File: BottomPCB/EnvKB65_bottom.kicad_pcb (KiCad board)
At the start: 2 copper layers, 320.8 x 99.3 mm, 7 parts

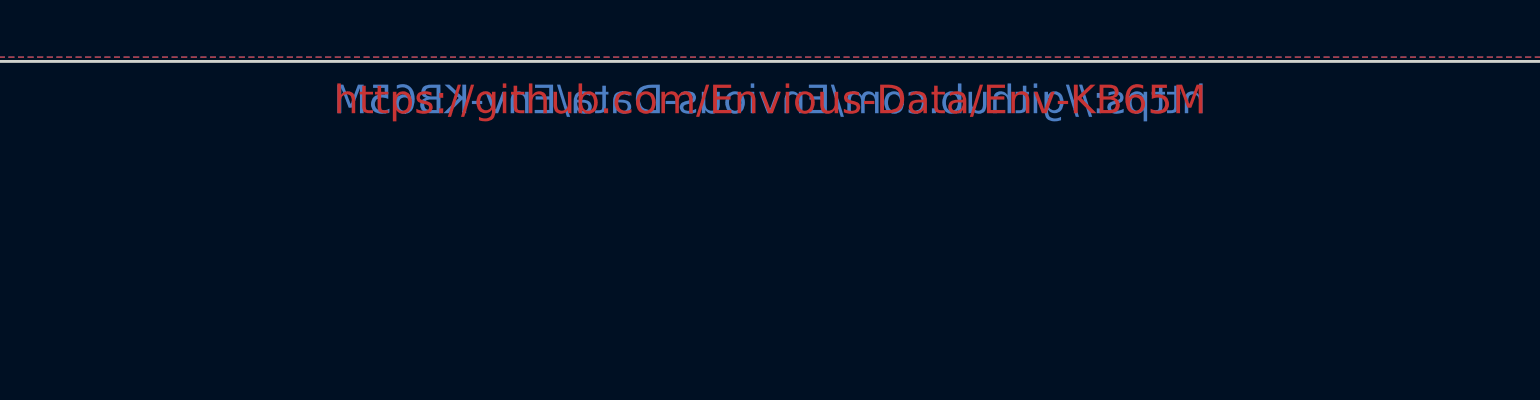
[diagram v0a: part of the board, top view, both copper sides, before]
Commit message: Swapped out mechboads logo for personal order
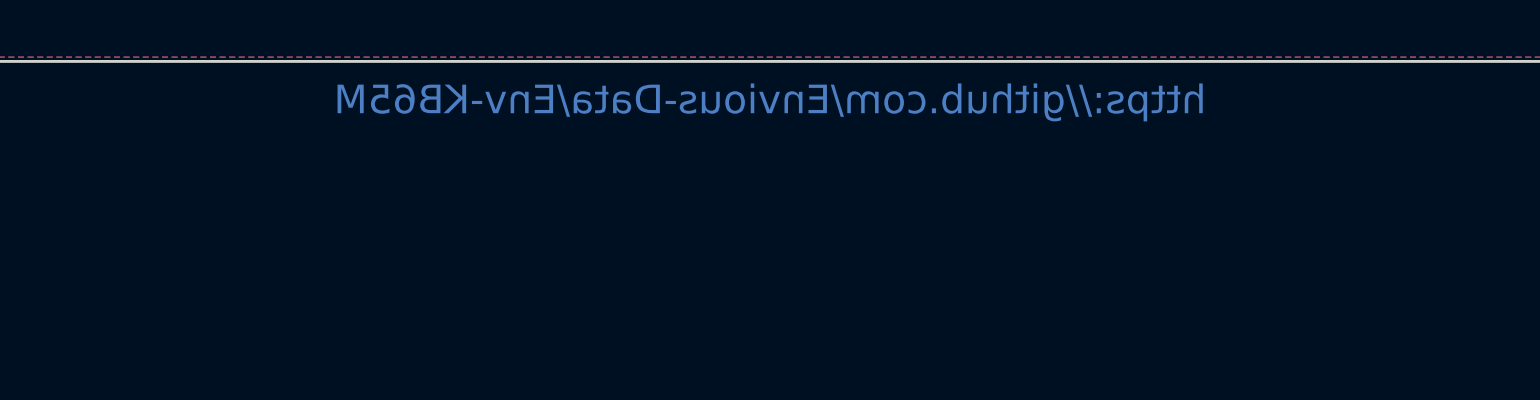
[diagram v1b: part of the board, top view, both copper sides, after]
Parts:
- Ref**: footprint MechboardsLogo:mechboardsLOGO_40mm -> Logo:logo
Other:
- board text added: "http://github.com/Envious-Data/Env-KB65M"
- board text removed: "http://Mechboards.co.uk"

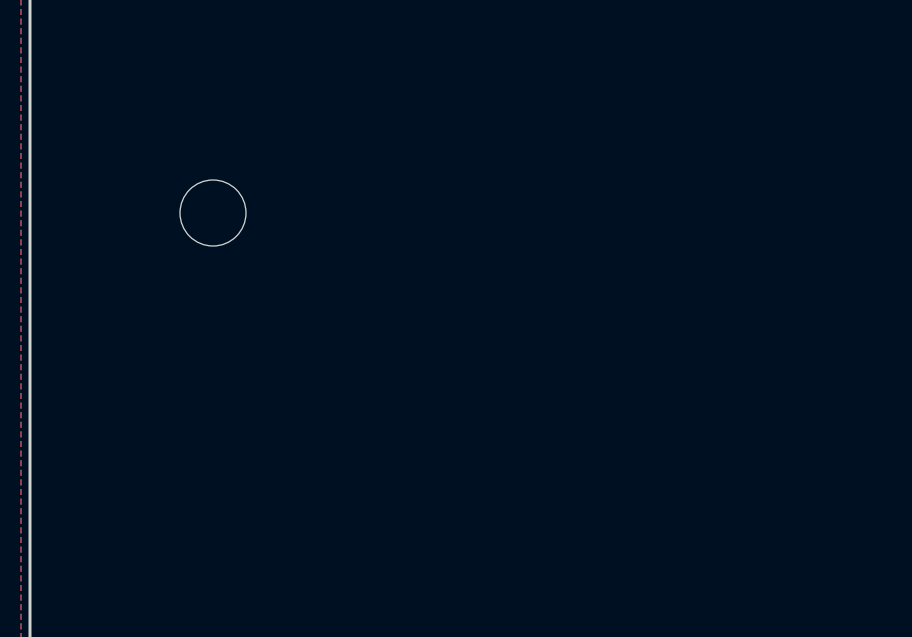
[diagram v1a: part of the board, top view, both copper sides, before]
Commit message: Added ANSI support, generated Gerbers and sent to JLCPCB
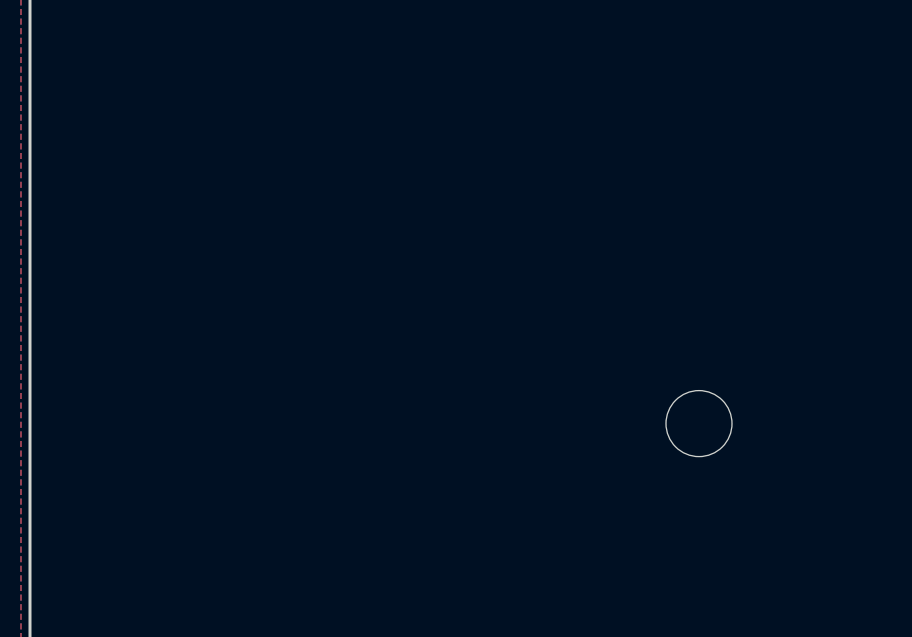
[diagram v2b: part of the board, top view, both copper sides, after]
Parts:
- removed H6: MountingHole, MountingHole:MountingHole_2.2mm_M2
- added H0: MountingHole, MountingHole:MountingHole_2.2mm_M2, F.Cu at (382.2, 101.0)
- moved H1 313.2 mm to (69.0, 101.0)
- moved H3 297.2 mm to (367.8, 180.5)
- moved H4 154.1 mm to (225.0, 122.5)
- moved H2 86.1 mm to (86.8, 185.2)
- moved H5 55.9 mm to (231.2, 178.0)

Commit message: Mount hole tweak to allow for switches to seat properly with a spacer installed
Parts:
- added H1: MountingHole, MountingHole:MountingHole_2.2mm_M2, F.Cu at (382.2, 101.0)
- added H2: MountingHole, MountingHole:MountingHole_2.2mm_M2, F.Cu at (69.0, 101.0)
- added H3: MountingHole, MountingHole:MountingHole_2.2mm_M2, F.Cu at (86.8, 185.2)
- added H6: MountingHole, MountingHole:MountingHole_2.2mm_M2, F.Cu at (210.6, 184.5)
- moved H4 154.1 mm to (367.8, 180.5)
- moved H5 56.5 mm to (224.9, 121.8)
- renumbered H0 to H1, H1 to H2, H2 to H3, H3 to H4
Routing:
- added copper zone on B.Cu, net (none)
- added copper zone on F.Cu, net (none)
- removed copper zone on B.Cu, net GND
- removed copper zone on F.Cu, net GND

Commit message: moved some mount holes a tiny bit and adjusted some traces for wider clearance.
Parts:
- removed the H1 at (382.2, 101.0) (x2)
- removed the H2 at (69.0, 101.0) (x2)
- removed the H3 at (86.8, 185.2) (x2)
- removed the H4 at (367.8, 180.5) (x2)
- removed the H5 at (224.9, 121.8)
- removed the H6 at (210.6, 184.5)
- added H1 (x3): MountingHole, MountingHole:MountingHole_2.2mm_M2, F.Cu at (382.2, 101.0)
- added H2 (x3): MountingHole, MountingHole:MountingHole_2.2mm_M2, F.Cu at (69.0, 101.0)
- added H3 (x3): MountingHole, MountingHole:MountingHole_2.2mm_M2, F.Cu at (86.8, 185.2)
- added H4 (x3): MountingHole, MountingHole:MountingHole_2.2mm_M2, F.Cu at (367.8, 178.2)
- added H5 (x2): MountingHole, MountingHole:MountingHole_2.2mm_M2, F.Cu at (224.9, 121.6)
- added H6 (x2): MountingHole, MountingHole:MountingHole_2.2mm_M2, F.Cu at (210.6, 184.5)
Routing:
- added copper zone on B.Cu, net gnd
- added copper zone on F.Cu, net gnd

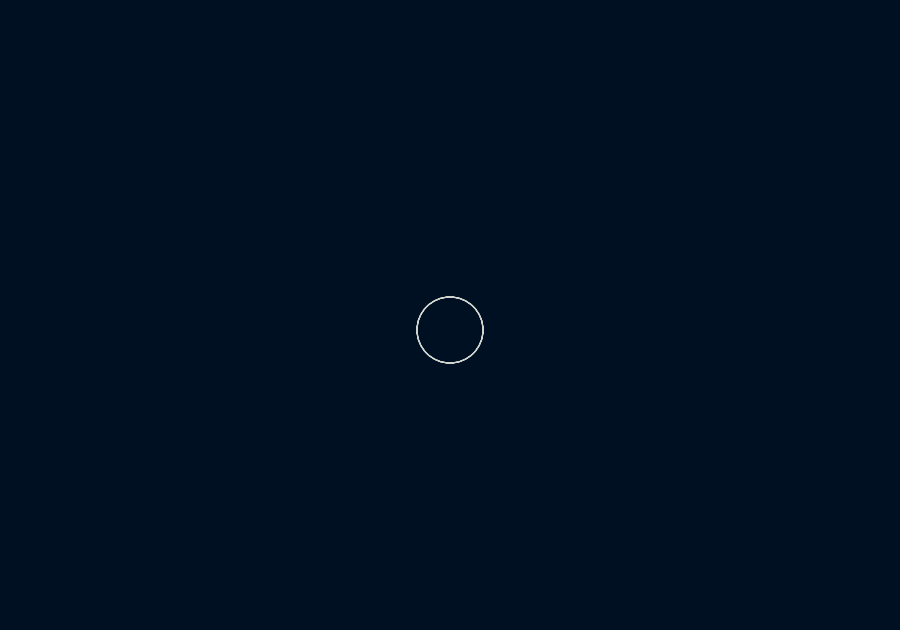
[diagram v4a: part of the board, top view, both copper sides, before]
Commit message: moved mount hole#6 up by 1mm and changed stabilizer cut out.
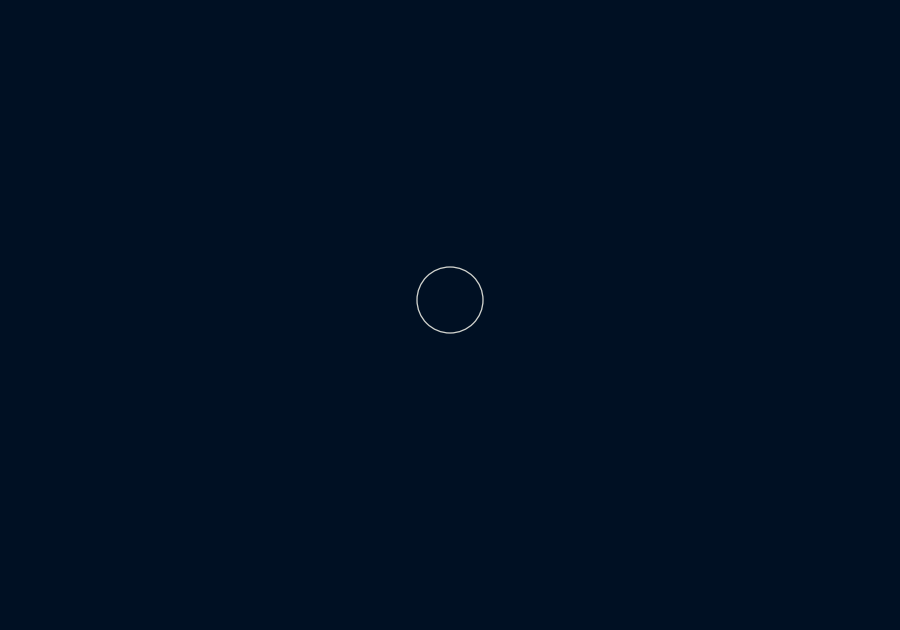
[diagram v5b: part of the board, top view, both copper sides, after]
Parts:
- removed the H6 at (210.6, 184.5)
- moved H6 1.00 mm to (210.6, 183.5)

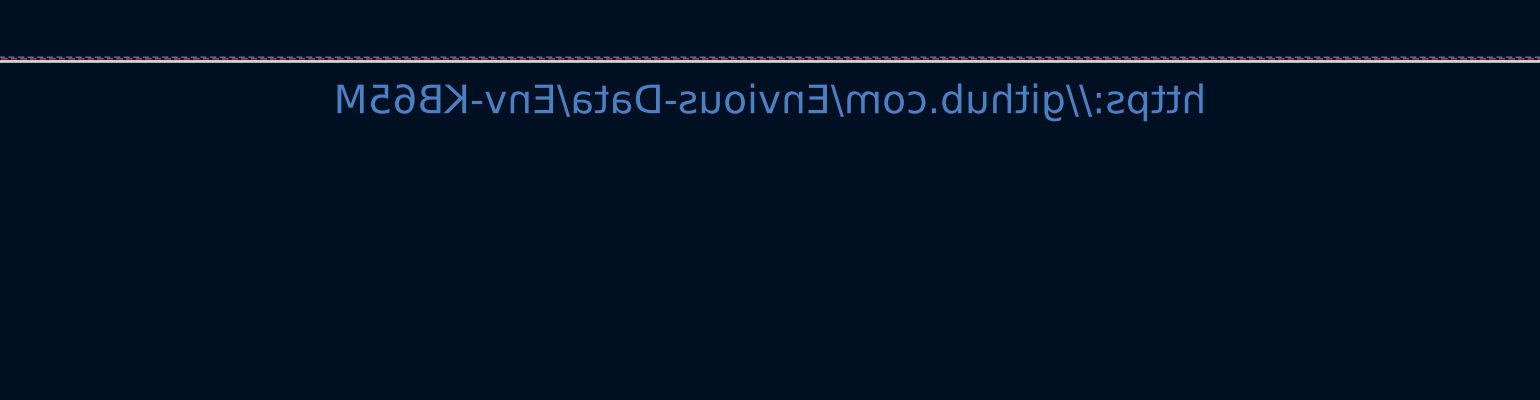
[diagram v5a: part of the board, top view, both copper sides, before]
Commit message: removed redundant url.
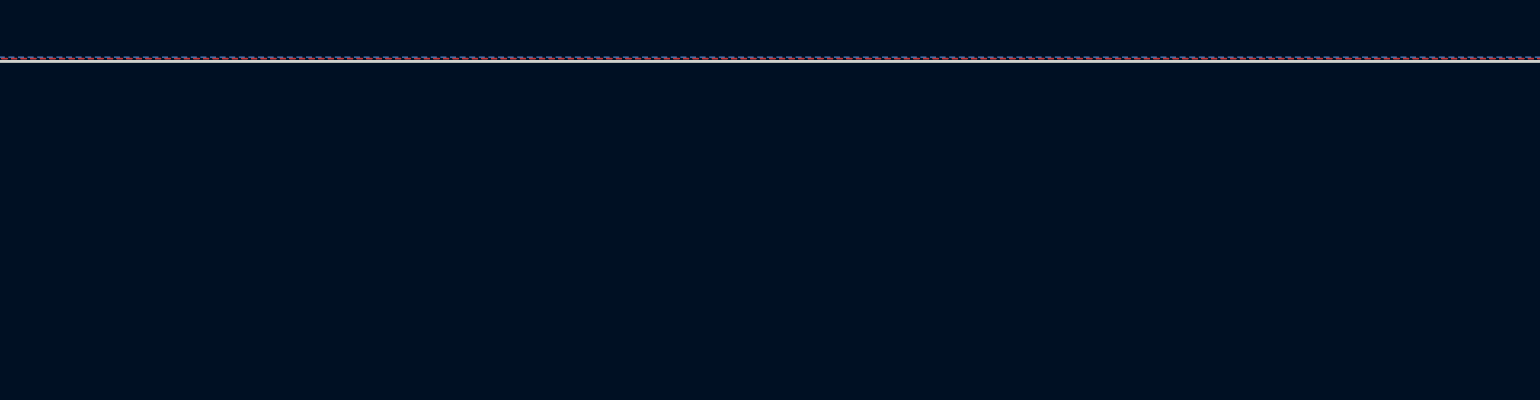
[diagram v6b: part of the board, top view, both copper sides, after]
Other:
- board text removed: "https://github.com/Envious-Data/Env-KB65M"

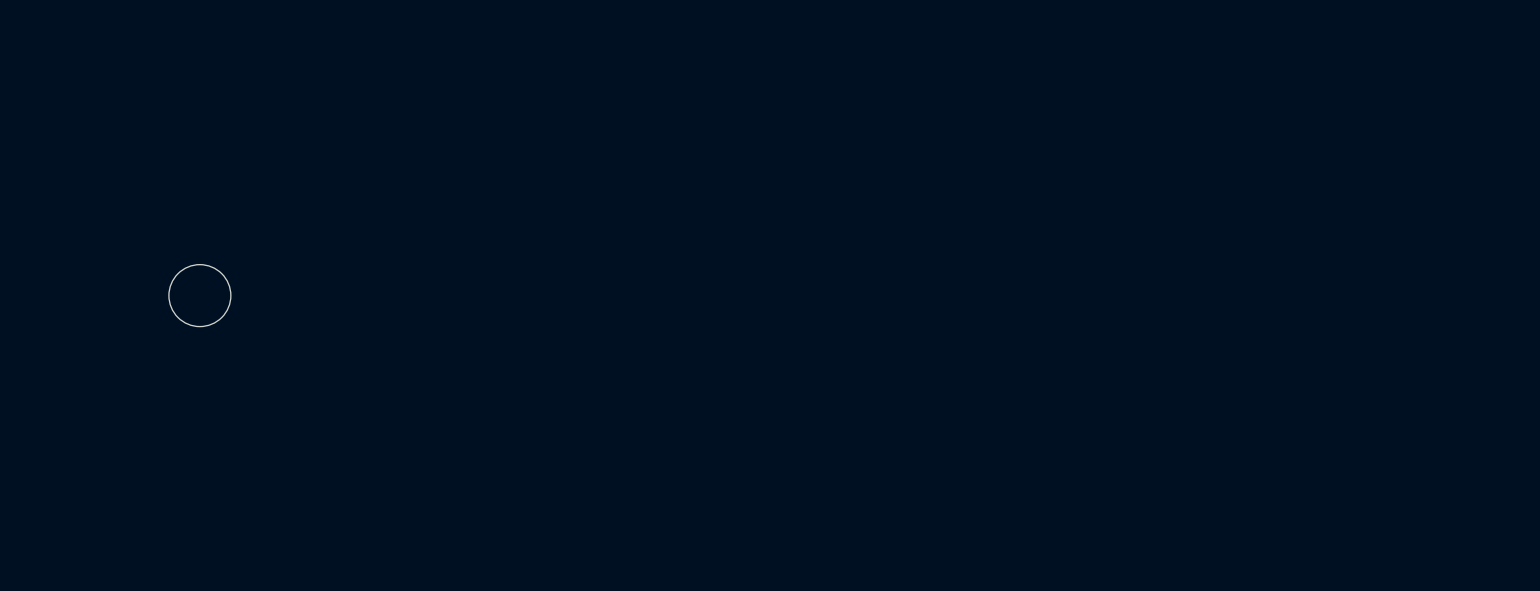
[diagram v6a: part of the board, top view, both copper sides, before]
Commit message: moved mount hole "H5" to the right by 40.5mm on all PCBs
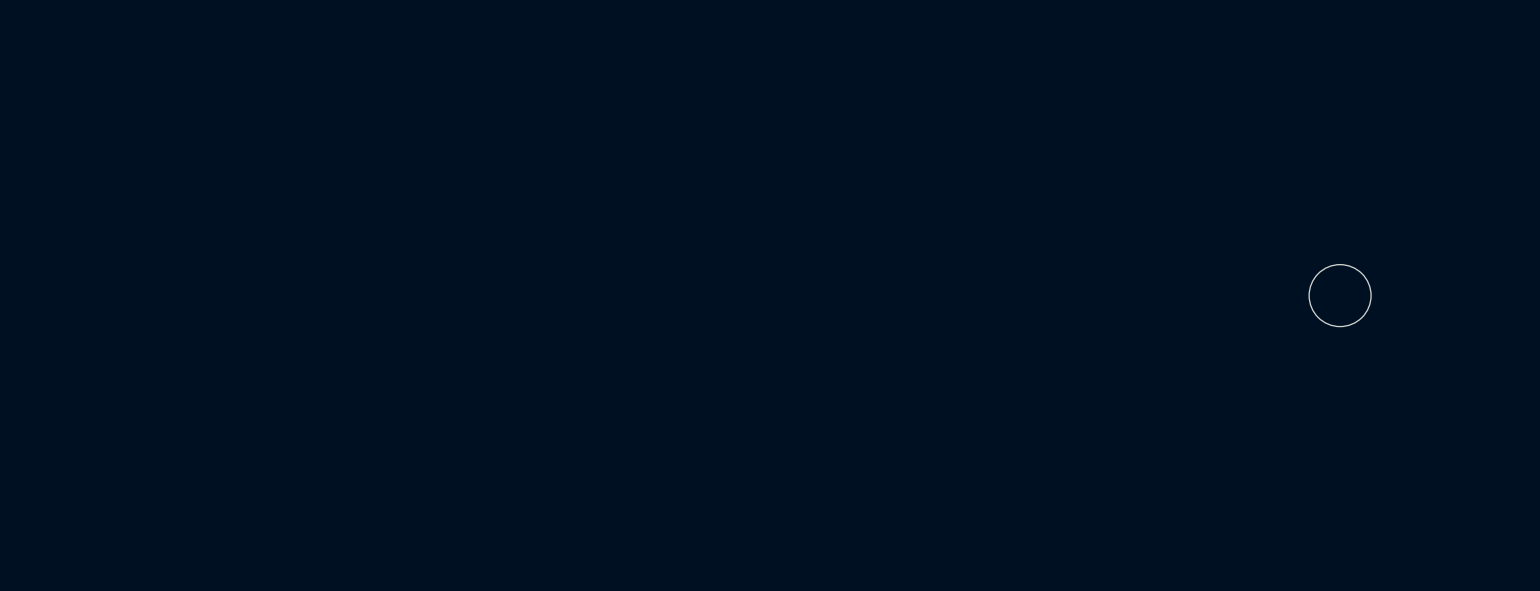
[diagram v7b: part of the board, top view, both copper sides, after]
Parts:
- moved H6 40.5 mm to (251.1, 183.5)

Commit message: replaced all mount holes with versions that have pads
I did this because the pcb can get scraped up if you take it apart a bunch of times to clean it, hopefully this mitigates that.
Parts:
- removed the H1 at (382.2, 101.0) (x2)
- removed the H2 at (69.0, 101.0) (x2)
- removed the H3 at (86.8, 185.2) (x2)
- removed the H4 at (367.8, 178.2) (x2)
- removed the H5 at (224.9, 121.6)
- H1, H2, H3, H4, H5, H6: footprint MountingHole:MountingHole_2.2mm_M2 -> MountingHole:MountingHole_2.2mm_M2_Pad
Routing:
- removed copper zone on B.Cu, net gnd
- removed copper zone on F.Cu, net gnd
